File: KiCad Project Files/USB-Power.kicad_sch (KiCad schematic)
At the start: 12 parts, among them U1 XC6206PxxxMR, U2 PRTR5V0U2X

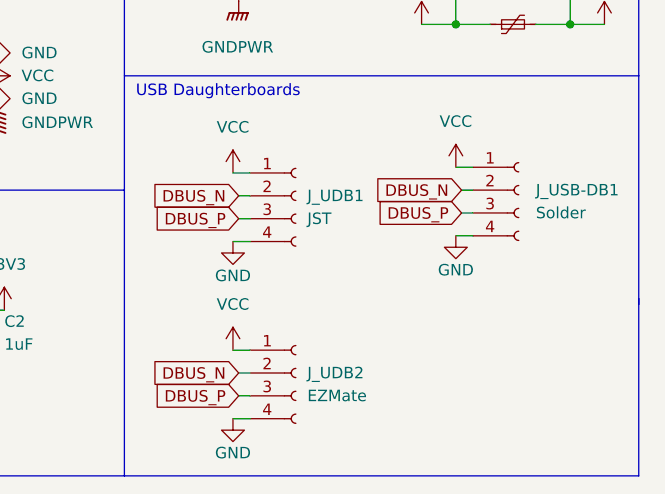
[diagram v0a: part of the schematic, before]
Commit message: added 225/275 support
2.75 stabs have break-away screw holes for compatibility with cases that need those areas of the PCB to be cut away
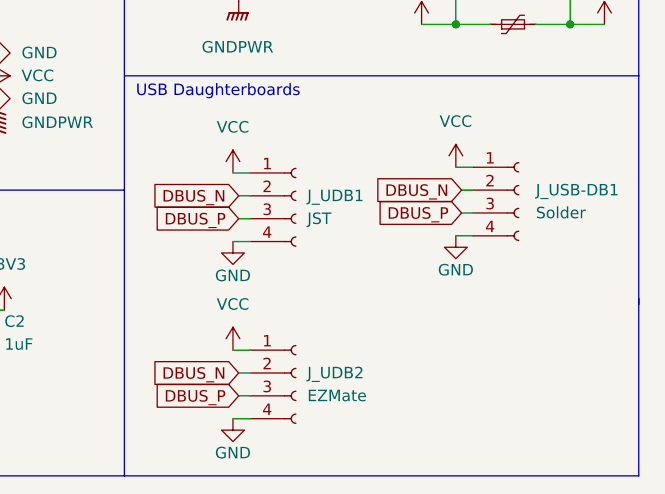
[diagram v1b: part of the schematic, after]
